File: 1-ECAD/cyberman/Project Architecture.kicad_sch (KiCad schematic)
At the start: 0 parts

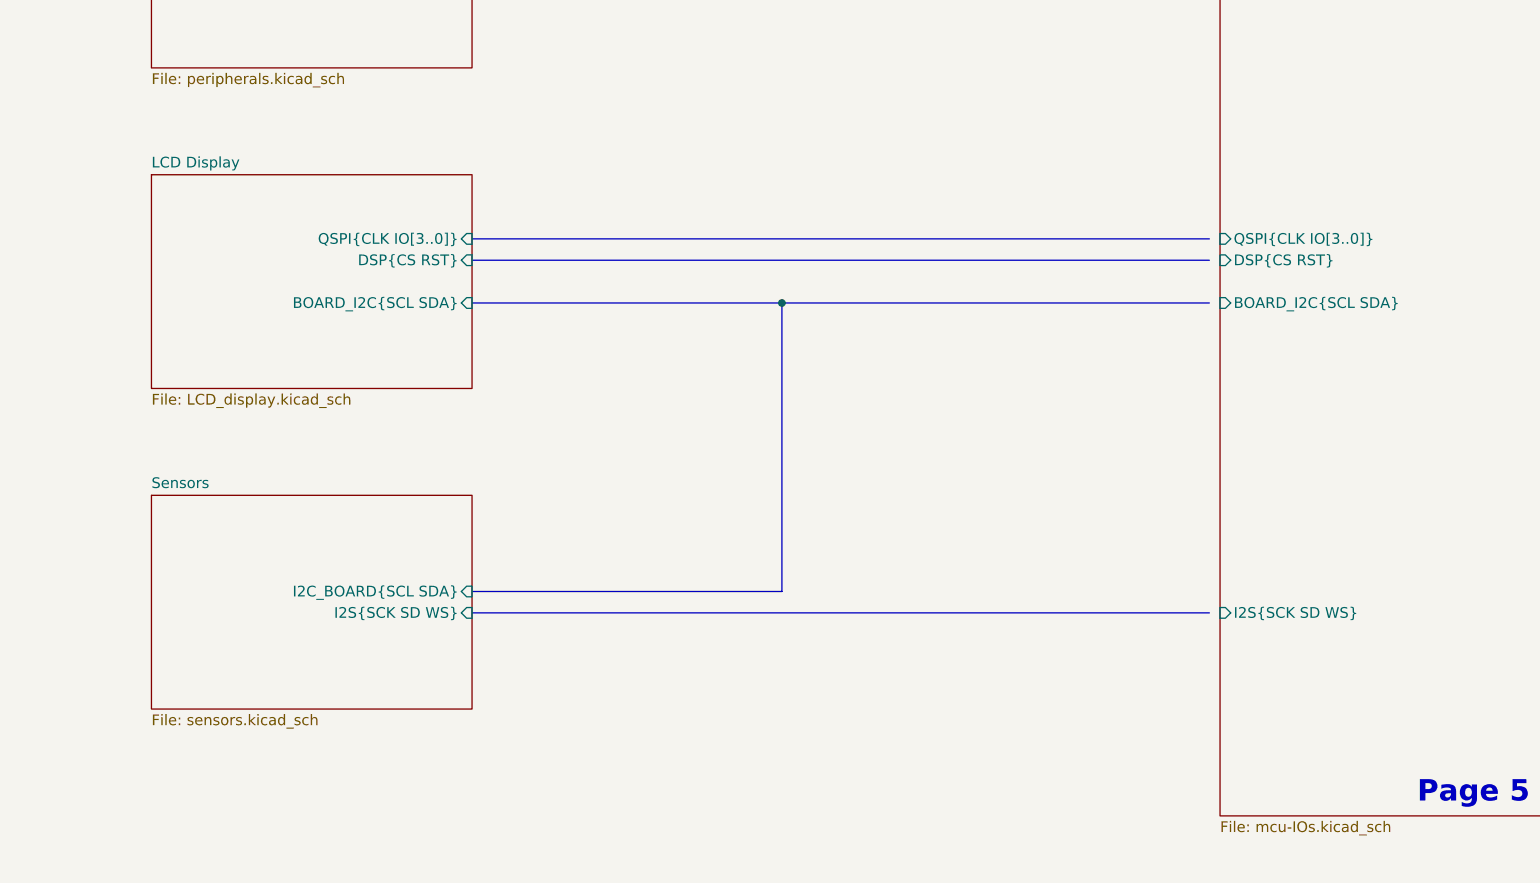
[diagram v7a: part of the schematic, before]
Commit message: new changes
close display page and peripheral schematic
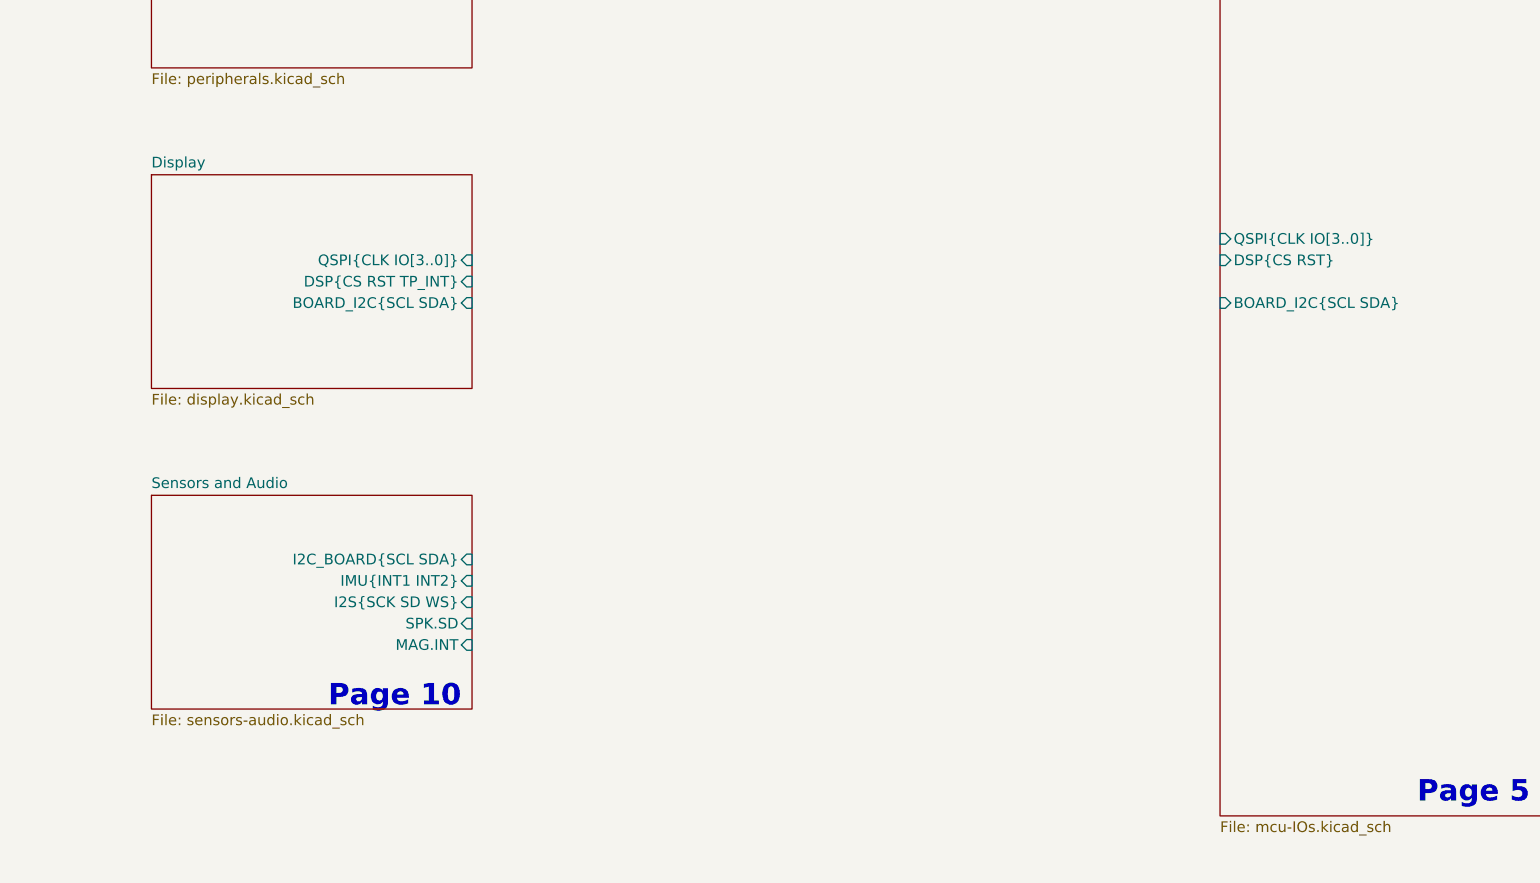
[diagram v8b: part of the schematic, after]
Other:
- sheet LCD Display renamed Display
- sheet Sensors renamed Sensors and Audio
- sheet Display: file LCD_display.kicad_sch -> display.kicad_sch
- sheet Display ports: added DSP{CS RST TP_INT}; removed DSP{CS RST}
- sheet MCU - IOs ports: added none; removed I2S{SCK SD WS}
- sheet Sensors and Audio: file sensors.kicad_sch -> sensors-audio.kicad_sch
- sheet Sensors and Audio ports: added IMU{INT1 INT2}, MAG.INT, SPK.SD; removed none
- note added: "Page 10"
- company: ${COMPANY} -> kode.
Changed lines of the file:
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@@
 	(title_block
 		(title "Project Architecture")
-		(date "Last Modified Date")
-		(rev "${REVISION}")
-		(company "${COMPANY}")
-	)
-	(junction
-		(at 163.83 142.24)
-		(diameter 0)
-		(color 0 0 0 0)
-	)
-	(bus
-		(pts
-			(xy 127 179.07) (xy 214.63 179.07)
-		)
-		(stroke
-			(width 0)
-			(type default)
-		)
+		(date "2024-12-11")
+		(rev "1.0")
+		(company "kode.")
 	)
 	(bus
@@
 	(bus
 		(pts
-			(xy 127 142.24) (xy 163.83 142.24)
-		)
-		(stroke
-			(width 0)
-			(type default)
-		)
-	)
-	(bus
-		(pts
-			(xy 163.83 142.24) (xy 214.63 142.24)
-		)
-		(stroke
-			(width 0)
-			(type default)
-		)
-	)
-	(bus
-		(pts
 			(xy 127 99.06) (xy 215.9 99.06)
-		)
-		(stroke
-			(width 0)
-			(type default)
-		)
-	)
-	(bus
-		(pts
-			(xy 127 134.62) (xy 214.63 134.62)
-		)
-		(stroke
-			(width 0)
-			(type default)
-		)
-	)
-	(bus
-		(pts
-			(xy 127 176.53) (xy 163.83 176.53)
-		)
-		(stroke
-			(width 0)
-			(type default)
-		)
-	)
-	(bus
-		(pts
-			(xy 163.83 142.24) (xy 163.83 176.53)
-		)
-		(stroke
-			(width 0)
-			(type default)
-		)
-	)
-	(bus
-		(pts
-			(xy 127 137.16) (xy 214.63 137.16)
 		)
 		(stroke
@@
 				(color 162 22 34 1)
 			)
+		)
+	)
+	(text "Page 10"
+		(exclude_from_sim no)
+		(at 125.73 190.5 0)
+		(effects
+			(font
+				(size 2.54 2.54)
+				(bold yes)
+				(color 100 70 50 1)
+			)
+			(justify right bottom)
+			(href "#5")
 		)
 	)
@@
 			(color 0 255 0 0.5000)
 		)
-		(property "Sheetname" "LCD Display"
+		(property "Sheetname" "Display"
 			(at 88.9 126.2884 0)
 			(effects
@@
 			)
 		)
-		(property "Sheetfile" "LCD_display.kicad_sch"
+		(property "Sheetfile" "display.kicad_sch"
 			(at 88.9 152.9846 0)
 			(effects
@@
 			)
 		)
-		(pin "DSP{CS RST}" input
+		(pin "DSP{CS RST TP_INT}" input
+			(at 127 139.7 0)
+			(effects
+				(font
+					(size 1.27 1.27)
+				)
+				(justify right)
+			)
+		)
+		(pin "QSPI{CLK IO[3..0]}" input
 			(at 127 137.16 0)
-			(effects
-				(font
-					(size 1.27 1.27)
-				)
-				(justify right)
-			)
-		)
-		(pin "QSPI{CLK IO[3..0]}" input
-			(at 127 134.62 0)
 			(effects
 				(font
@@
 			(color 255 0 255 0.5000)
 		)
-		(property "Sheetname" "Sensors"
+		(property "Sheetname" "Sensors and Audio"
 			(at 88.9 164.3884 0)
 			(effects
@@
 			)
 		)
-		(property "Sheetfile" "sensors.kicad_sch"
+		(property "Sheetfile" "sensors-audio.kicad_sch"
 			(at 88.9 191.0846 0)
 			(effects
@@
 			)
 		)
+		(pin "IMU{INT1 INT2}" input
+			(at 127 175.26 0)
+			(effects
+				(font
+					(size 1.27 1.27)
+				)
+				(justify right)
+			)
+		)
+		(pin "SPK.SD" input
+			(at 127 180.34 0)
+			(effects
+				(font
+					(size 1.27 1.27)
+				)
+				(justify right)
+			)
+		)
+		(pin "MAG.INT" input
+			(at 127 182.88 0)
+			(effects
+				(font
+					(size 1.27 1.27)
+				)
+				(justify right)
+			)
+		)
+		(pin "I2S{SCK SD WS}" input
+			(at 127 177.8 0)
+			(effects
+				(font
+					(size 1.27 1.27)
+				)
+				(justify right)
+			)
+		)
 		(pin "I2C_BOARD{SCL SDA}" input
-			(at 127 176.53 0)
-			(effects
-				(font
-					(size 1.27 1.27)
-				)
-				(justify right)
-			)
-		)
-		(pin "I2S{SCK SD WS}" input
-			(at 127 179.07 0)
+			(at 127 172.72 0)
 			(effects
 				(font
@@
 			)
 		)
-		(pin "I2S{SCK SD WS}" input
-			(at 215.9 179.07 180)
-			(effects
-				(font
-					(size 1.27 1.27)
-				)
-				(justify left)
-			)
-		)
